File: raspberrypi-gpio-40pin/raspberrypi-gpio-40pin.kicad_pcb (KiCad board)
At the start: 2 copper layers, 65 x 56 mm, 5 parts, among them P1 Conn_02x20_Odd_Even

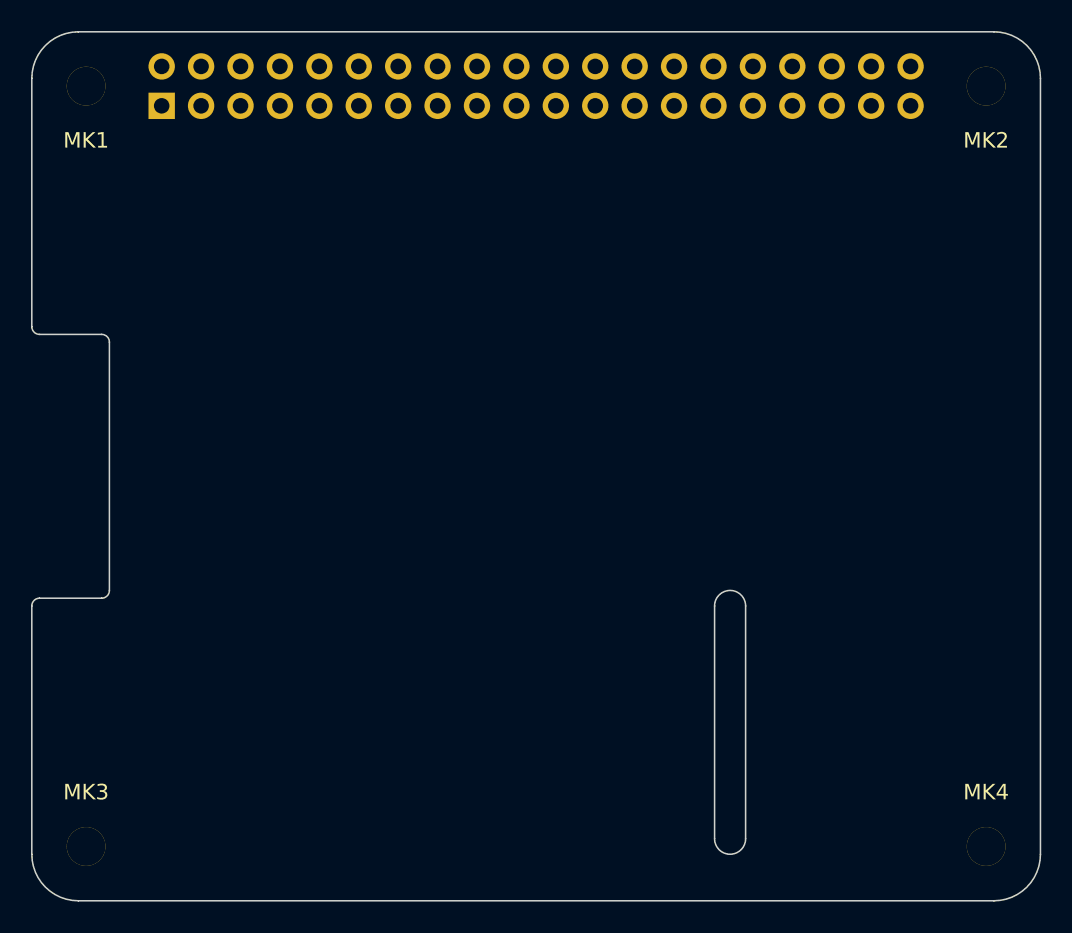
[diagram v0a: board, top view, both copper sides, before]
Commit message: Update rasperrypi-gpio-40pin symbols and footprints
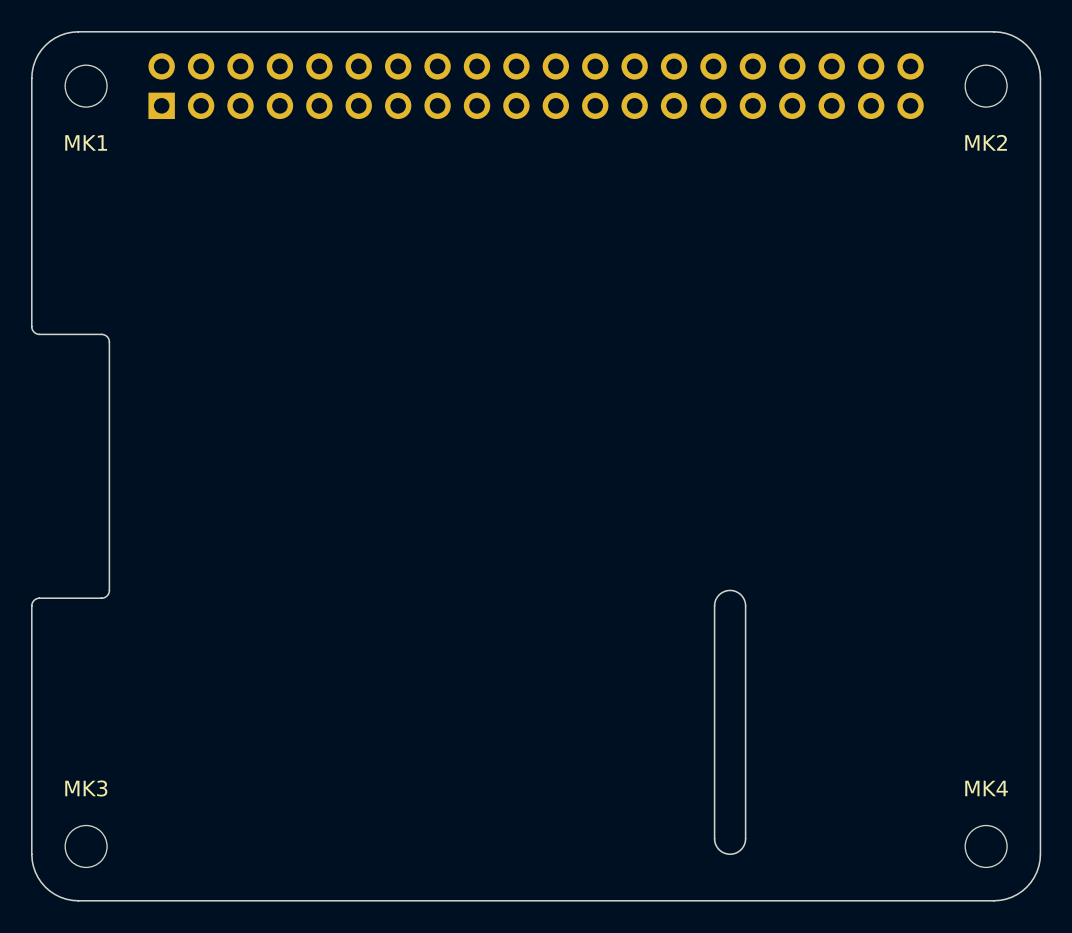
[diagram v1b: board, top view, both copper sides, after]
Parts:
- MK1, MK2, MK3, MK4: footprint Mounting_Holes:MountingHole_2-5mm -> MountingHole:MountingHole_2.7mm_M2.5
- P1: footprint Socket_Strips:Socket_Strip_Straight_2x20_Pitch2.54mm -> Connector_PinSocket_2.54mm:PinSocket_2x20_P2.54mm_Vertical
